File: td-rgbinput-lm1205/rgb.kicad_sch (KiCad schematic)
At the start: 57 parts, among them J1 Conn_01x10_Socket, J16 Conn_01x06_Male, J17 Conn_01x06_Male, J5 DB15_Female_HighDensity, U11 24LC08, U18 LM1205, U19 LMH1980, U2 74HCT14, U26 MCP4728, U27 MCP4728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

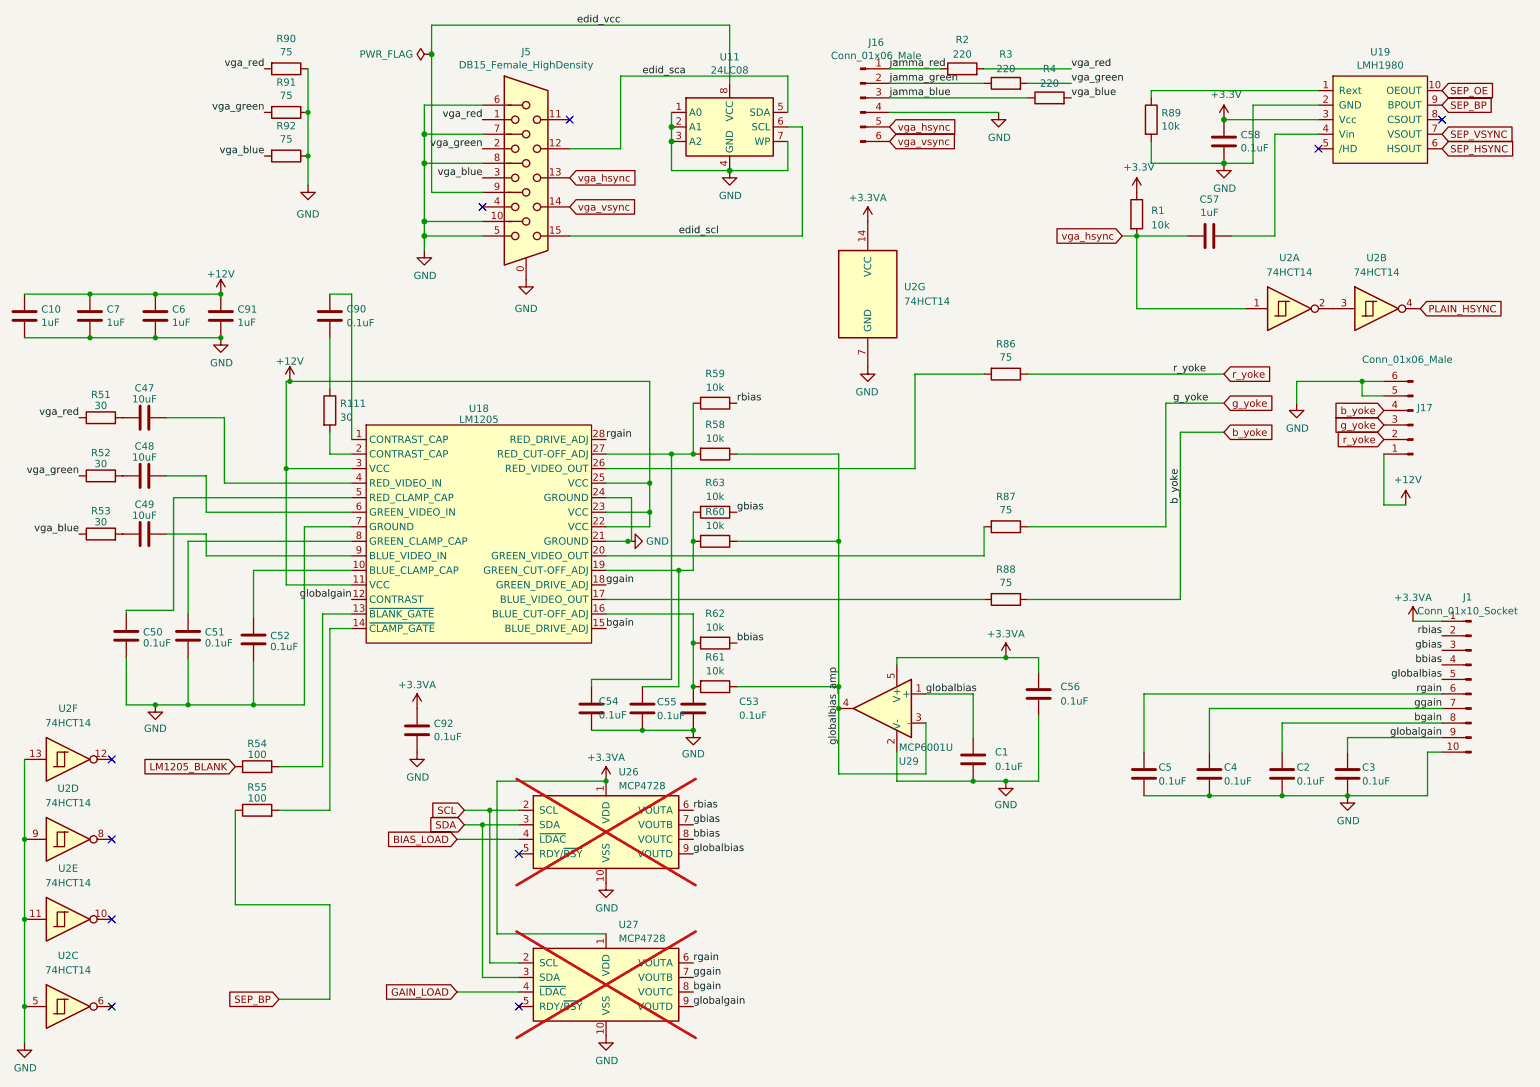
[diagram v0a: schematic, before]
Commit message: Update td-rgbinput-lm1205 to add a linear regulator.
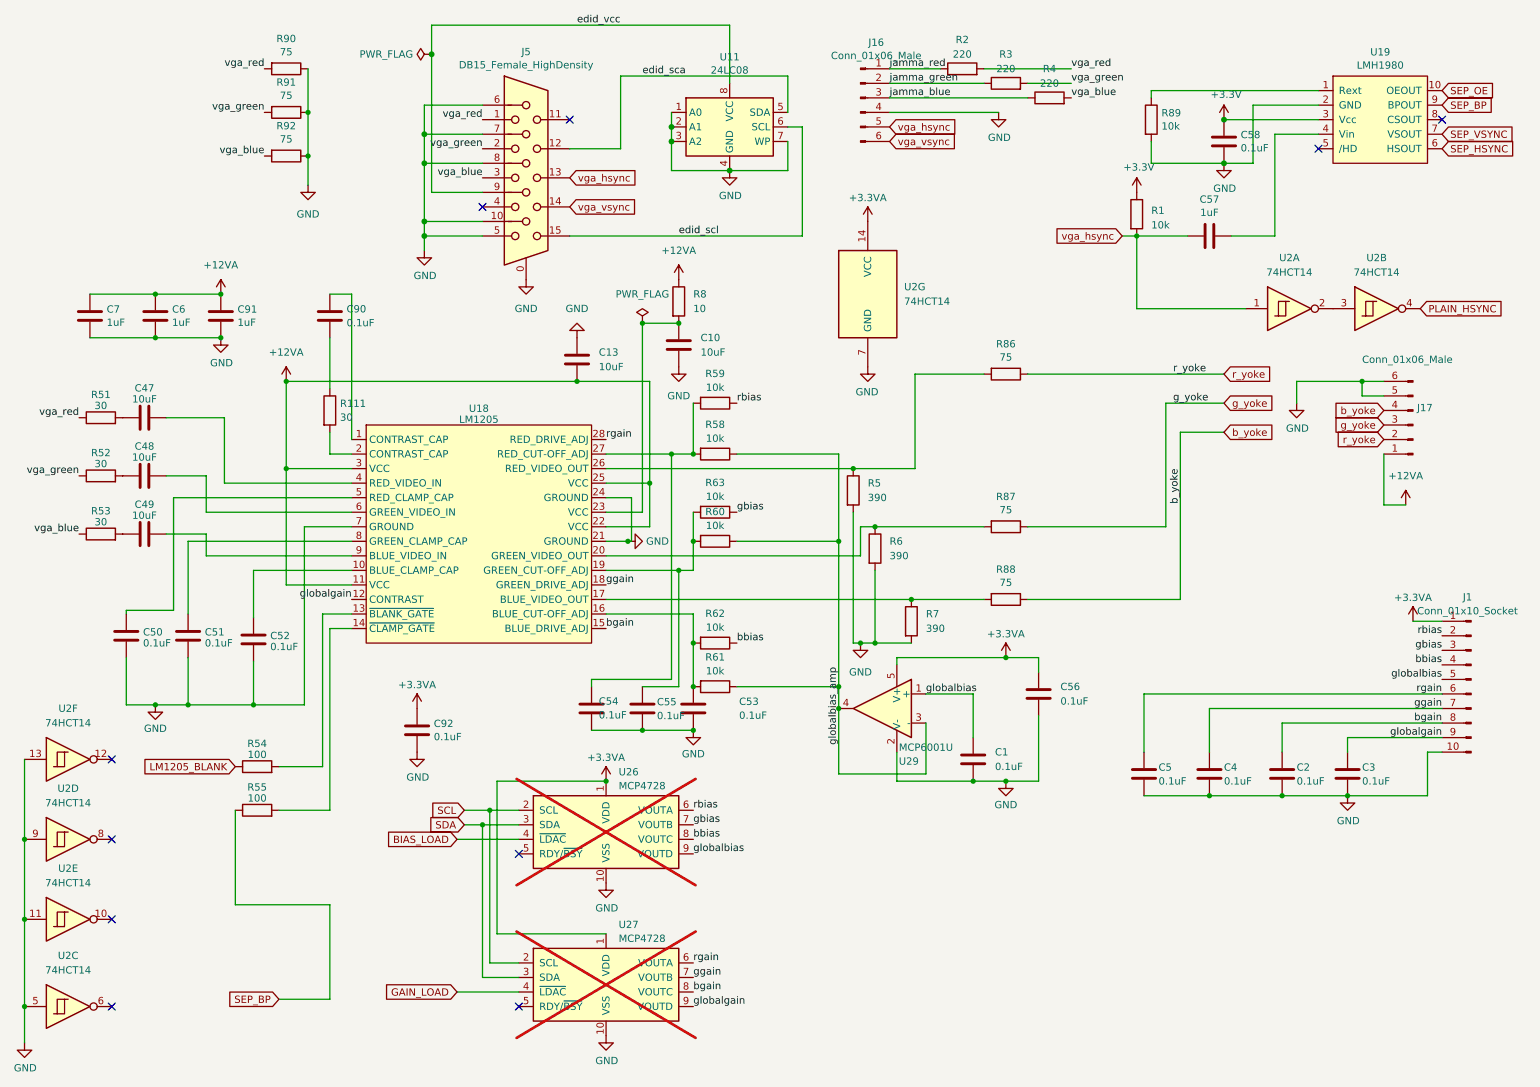
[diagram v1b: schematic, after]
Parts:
- added C13: 10uF, Capacitor_SMD:C_0805_2012Metric, symbol Device:C
- added R5, R6, R7: 390, Resistor_SMD:R_0805_2012Metric, symbol Device:R
- added R8: 10, Resistor_SMD:R_0805_2012Metric, symbol Device:R
- C10: value 1uF -> 10uF; Digikey 1276-1066-1-ND -> (none)
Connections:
- net GND: now also C13.2, R5.2, R6.2, R7.2
- net at R86.2, U18.26 (RED_VIDEO_OUT): now also R5.1
- net at R87.2, U18.20 (GREEN_VIDEO_OUT): now also R6.1
- net at R88.2, U18.17 (BLUE_VIDEO_OUT): now also R7.1
- net +12V renamed +12VA
- net +12VA: now also C13.1, R8.1; no longer C10.1, U18.23 (VCC)
- new net: C10.1, R8.2, U18.23 (VCC)

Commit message: bunch of random updates
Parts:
- C10, C13: Digikey (none) -> 490-10516-1-ND
- J5: Digikey AE11024-ND -> L77HDE15SD1CH4FVGA-ND
- R5, R6, R7: Digikey (none) -> 311-390CRCT-ND
- R8: Digikey (none) -> 311-10.0CRCT-ND
- U18: Digikey (none) -> 3M5481-ND
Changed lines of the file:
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@@
 			)
 		)
-		(property "Digikey" " AE11024-ND "
+		(property "Digikey" "L77HDE15SD1CH4FVGA-ND"
 			(at 104.14 41.91 0)
 			(effects
@@
 			)
 		)
+		(property "Digikey" "3M5481-ND"
+			(at 76.2 85.09 0)
+			(effects
+				(font
+					(size 1.27 1.27)
+				)
+				(hide yes)
+			)
+		)
 		(pin "1"
 		)
@@
 			)
 		)
+		(property "Digikey" "311-390CRCT-ND"
+			(at 171.45 119.38 0)
+			(effects
+				(font
+					(size 1.27 1.27)
+				)
+				(hide yes)
+			)
+		)
 		(pin "2"
 		)
@@
 			)
 		)
+		(property "Digikey" "311-390CRCT-ND"
+			(at 161.29 96.52 0)
+			(effects
+				(font
+					(size 1.27 1.27)
+				)
+				(hide yes)
+			)
+		)
 		(pin "2"
 		)
@@
 			)
 		)
+		(property "Digikey" "311-10.0CRCT-ND"
+			(at 130.81 63.5 0)
+			(effects
+				(font
+					(size 1.27 1.27)
+				)
+				(hide yes)
+			)
+		)
 		(pin "1"
 		)
@@
 			)
 		)
+		(property "Digikey" "490-10516-1-ND"
+			(at 113.03 73.66 0)
+			(effects
+				(font
+					(size 1.27 1.27)
+				)
+				(hide yes)
+			)
+		)
 		(pin "2"
 		)
@@
 			)
 		)
+		(property "Digikey" "311-390CRCT-ND"
+			(at 165.1 106.68 0)
+			(effects
+				(font
+					(size 1.27 1.27)
+				)
+				(hide yes)
+			)
+		)
 		(pin "2"
 		)
@@
 			(at 130.81 71.12 0)
 			(effects
+				(font
+					(size 1.27 1.27)
+				)
+				(hide yes)
+			)
+		)
+		(property "Digikey" "490-10516-1-ND"
+			(at 130.81 71.12 0)
+			(effects
